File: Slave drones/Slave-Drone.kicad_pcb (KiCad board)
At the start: 4 copper layers, 32 x 32 mm, 46 parts, among them J1 Conn_01x02, J2 Conn_01x02, J3 Conn_01x02, J4 Conn_01x02, J5 USB_C_Receptacle_USB2.0_16P, J6 Conn_01x02, SW1 SW_Push, SW2 SW_Push, U1 MPU6500, U2 QMC5883L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

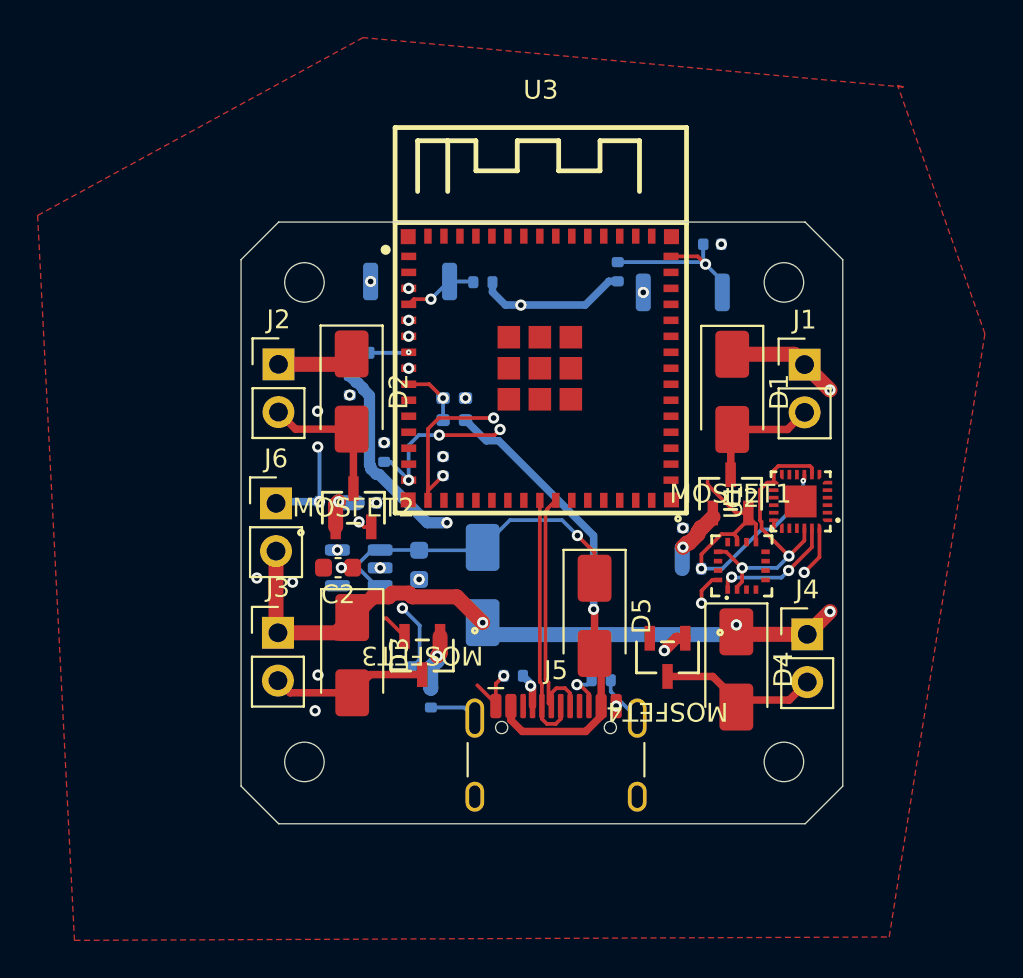
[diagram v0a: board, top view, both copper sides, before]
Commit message: removed any vias that were on pads
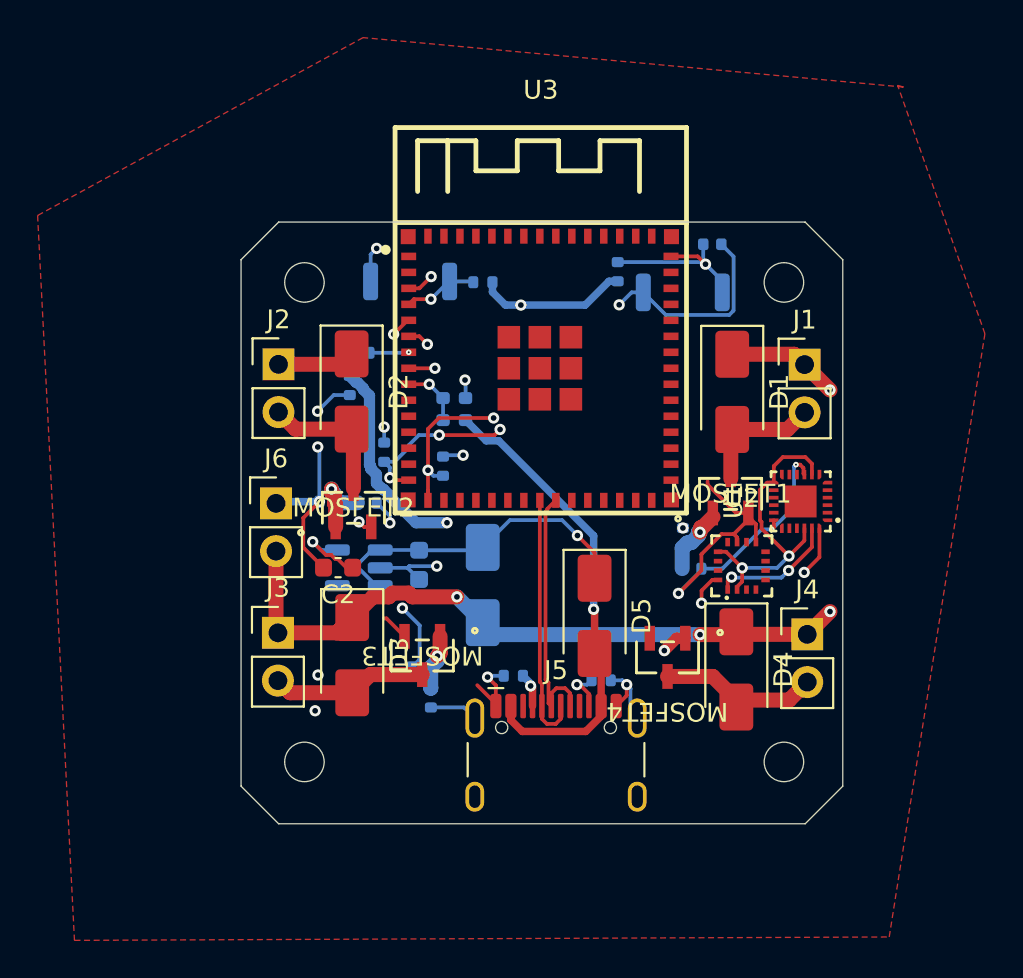
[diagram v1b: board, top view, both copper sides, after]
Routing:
- net GND: track 42.5 -> 71.8 mm, vias 20 -> 15
- net +3.3V: track 24.4 -> 32.0 mm, vias 8 -> 7
- net Net-(U3-IO1): track 10.7 -> 13.5 mm
- net Net-(U3-IO2): track 18.4 -> 20.6 mm
- net /Motor1: track 2.43 -> 3.95 mm

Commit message: Updated via hole size
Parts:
- renumbered REF** to M1, REF** to M2, REF** to M3, REF** to M4
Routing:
- net +3.3V: track 32.0 -> 77.4 mm
- net Net-(U3-IO2): track 20.6 -> 22.0 mm
- net GND: track 71.8 -> 73.0 mm
- net /SCL: track 31.8 -> 31.3 mm
